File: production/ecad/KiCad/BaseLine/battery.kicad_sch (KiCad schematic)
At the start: 16 parts, among them IC1 AP7362-33SP-13 (3.3V LDO), J2 Conn_01x02, Q1 Si3456DDV, U7 LTC3872ETS8TRMPBF

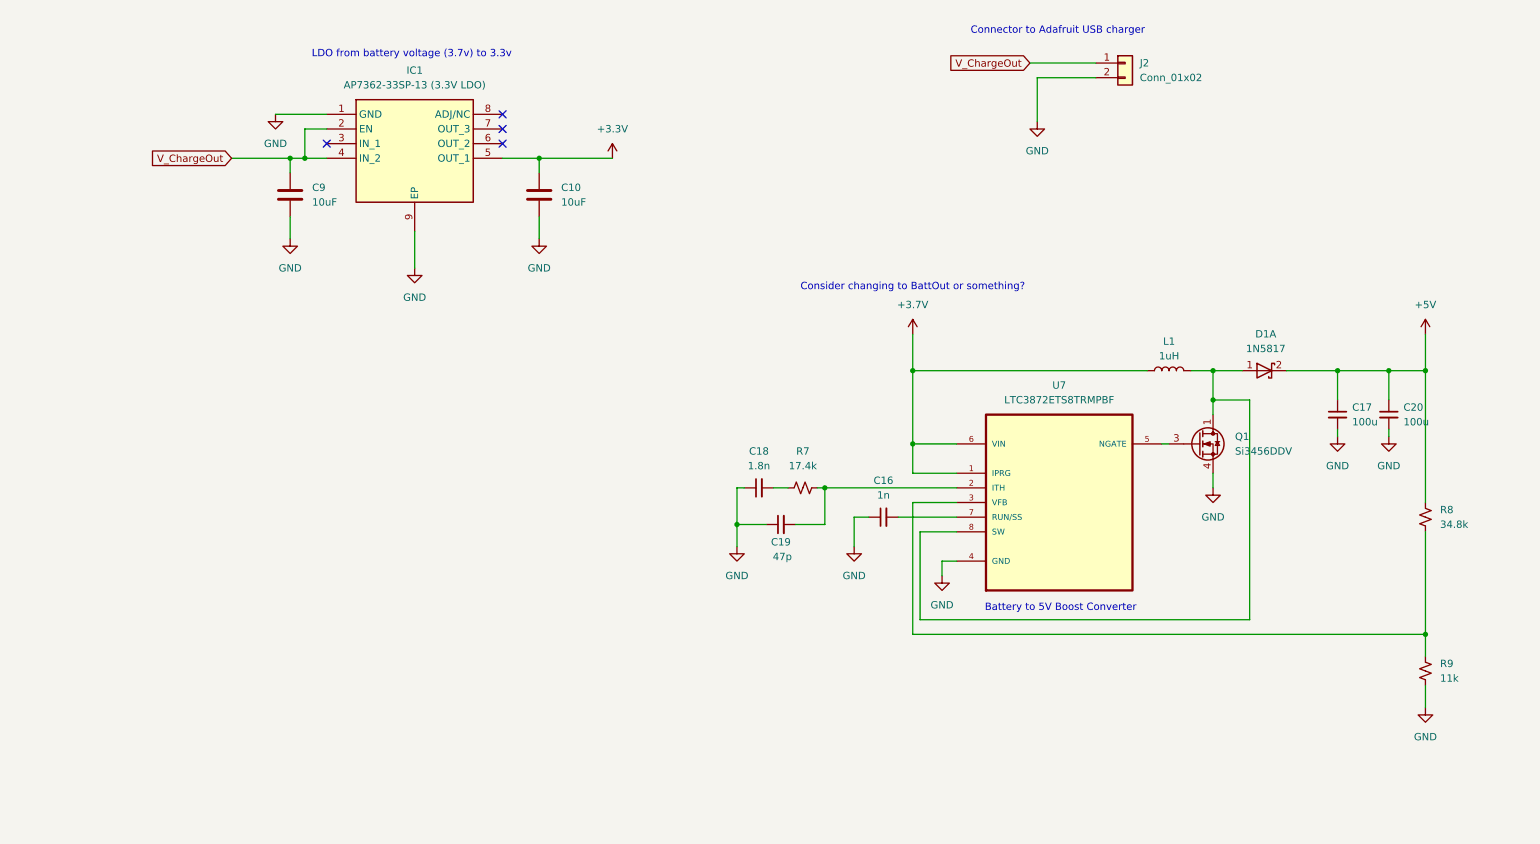
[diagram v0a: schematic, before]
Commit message: Added some zener diodes to BMS
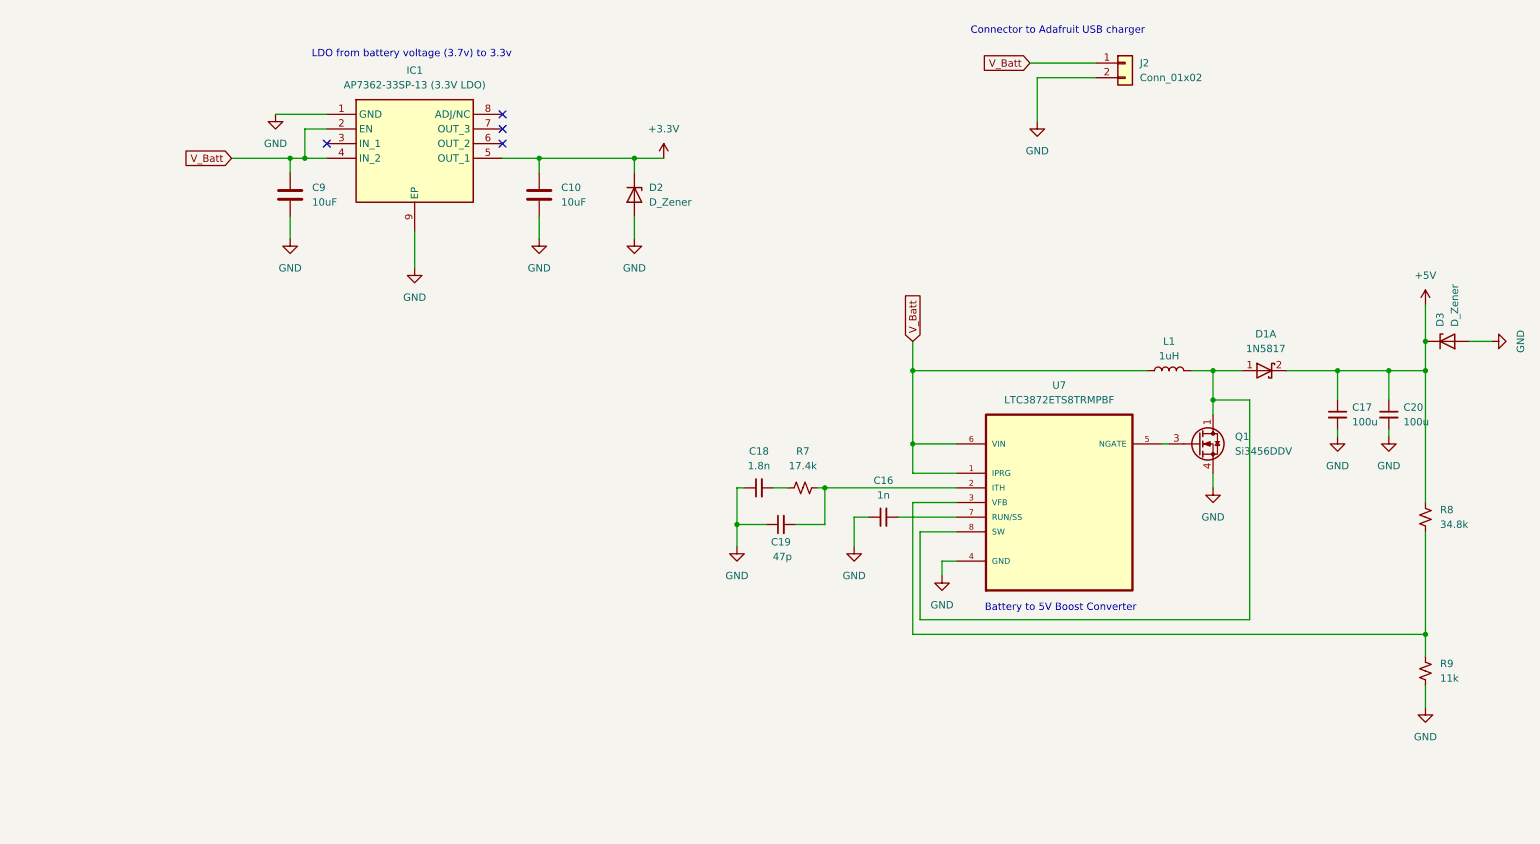
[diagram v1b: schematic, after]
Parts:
- added D2, D3: D_Zener, symbol Device:D_Zener
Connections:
- net V_ChargeOut is gone; now on net V_Batt: C9.2, IC1.2 (EN), IC1.4 (IN_2), J2.1 (Pin_1)
- net +3.3V: now also D2.1 (K)
- net +5V: now also D3.1 (K)
- net GND: now also D2.2 (A), D3.2 (A)
- net +3.7V renamed V_Batt
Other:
- note removed: "Consider changing to BattOut or something?"

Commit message: Started adding power button on BMS but needs additional info.
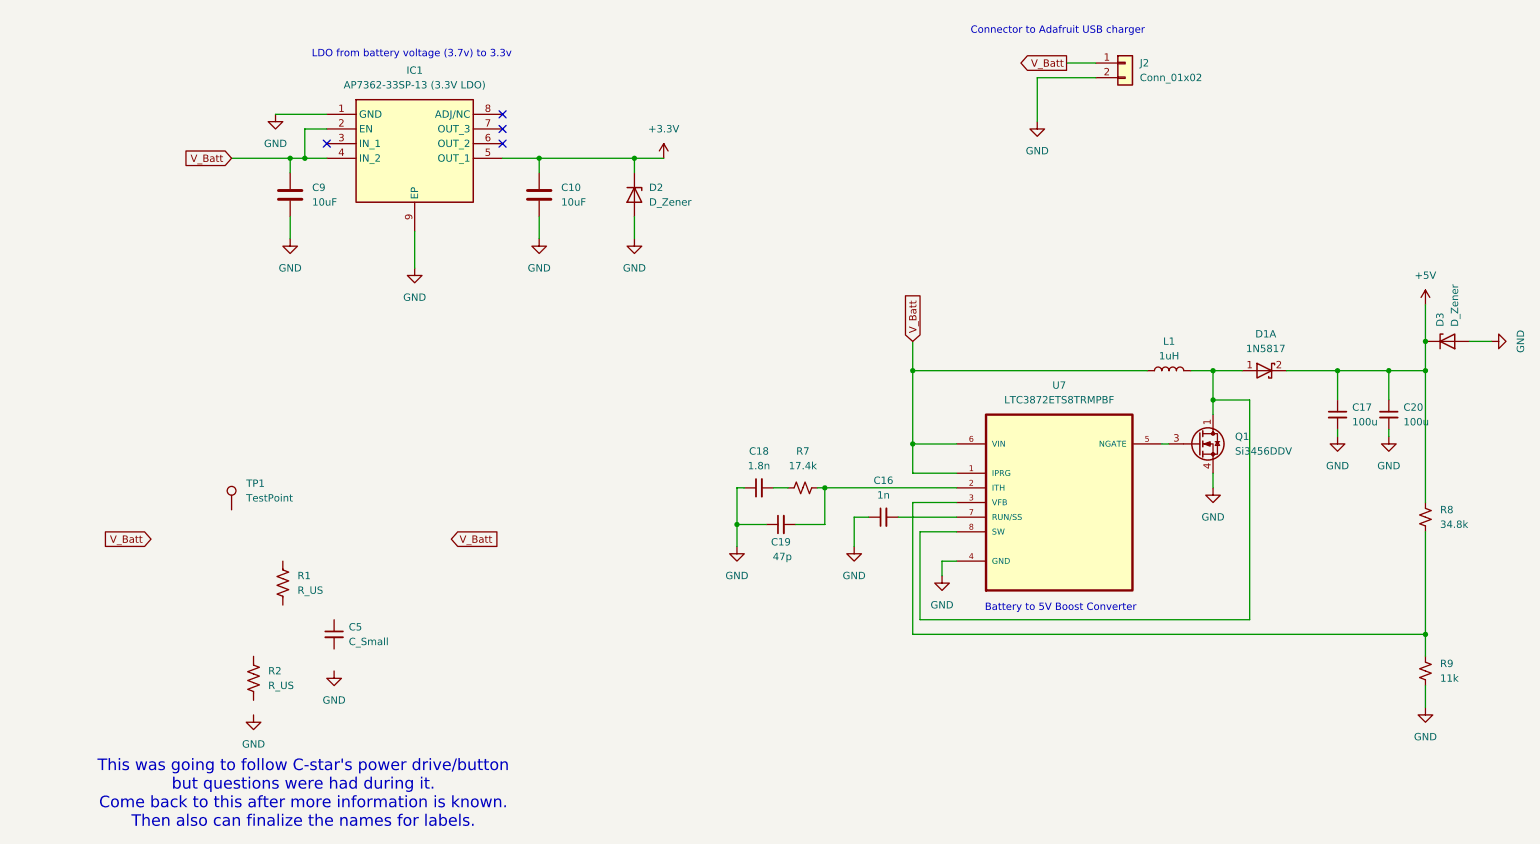
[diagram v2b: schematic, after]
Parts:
- added C5: C_Small, symbol Device:C_Small
- added R1, R2: R_US, symbol Device:R_US
- added TP1: TestPoint, symbol Connector:TestPoint
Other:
- note added: "This was going to follow C-star's power drive/button but questions were had during it. Come back to this after more information is known. Then also can finalize the names for labels."

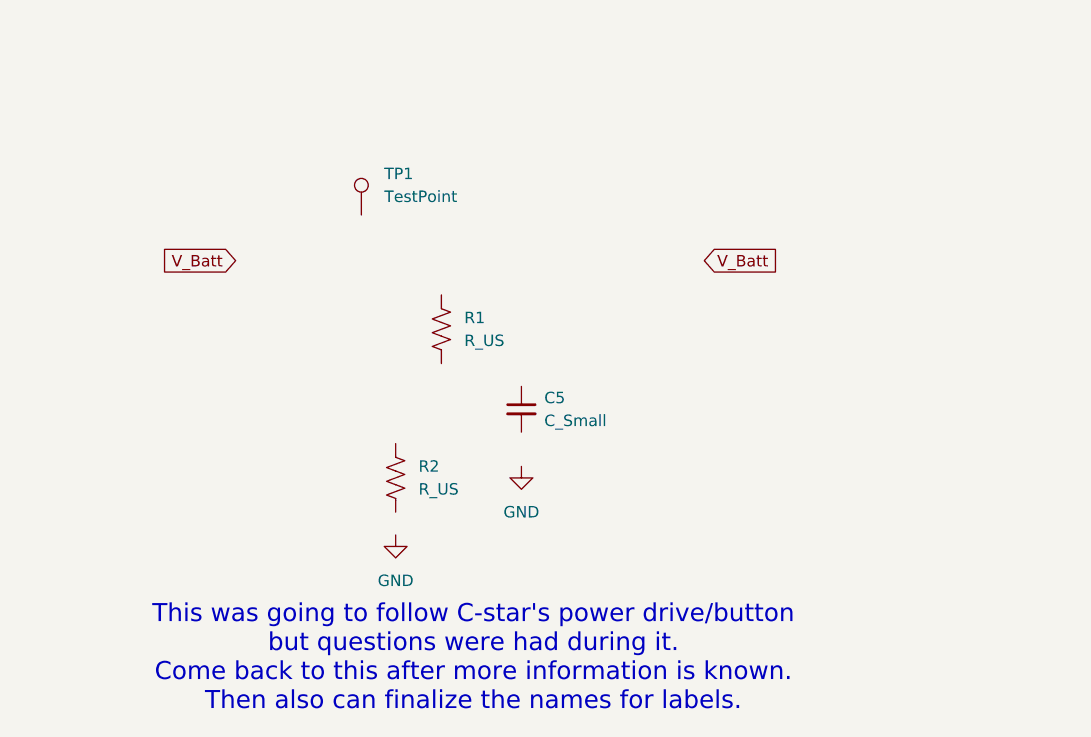
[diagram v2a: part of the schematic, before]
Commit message: MCU connections and matching names
matched the global net names of all the sensor connections with the MCU. Added an IO sheet for the power button
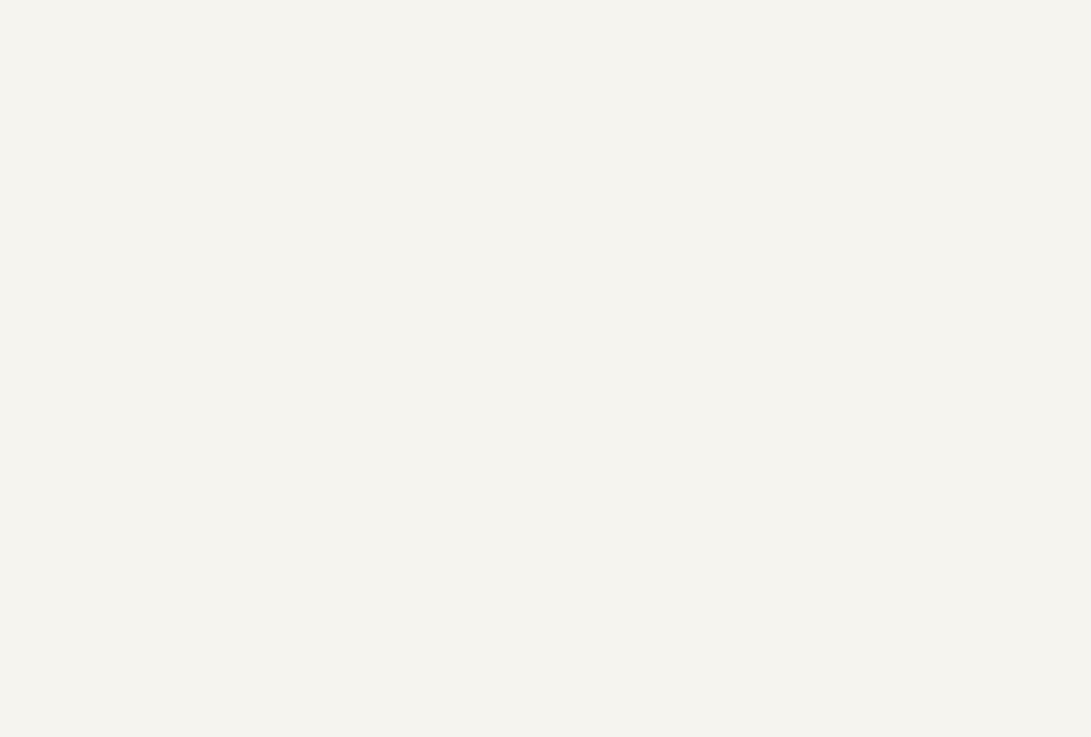
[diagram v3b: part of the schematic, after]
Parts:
- removed C5: C_Small, symbol Device:C_Small
- removed R1, R2: R_US, symbol Device:R_US
- removed TP1: TestPoint, symbol Connector:TestPoint
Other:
- note removed: "This was going to follow C-star's power drive/button but questions were had during it. Come back to this after more information is known. Then also can finalize the names for labels."

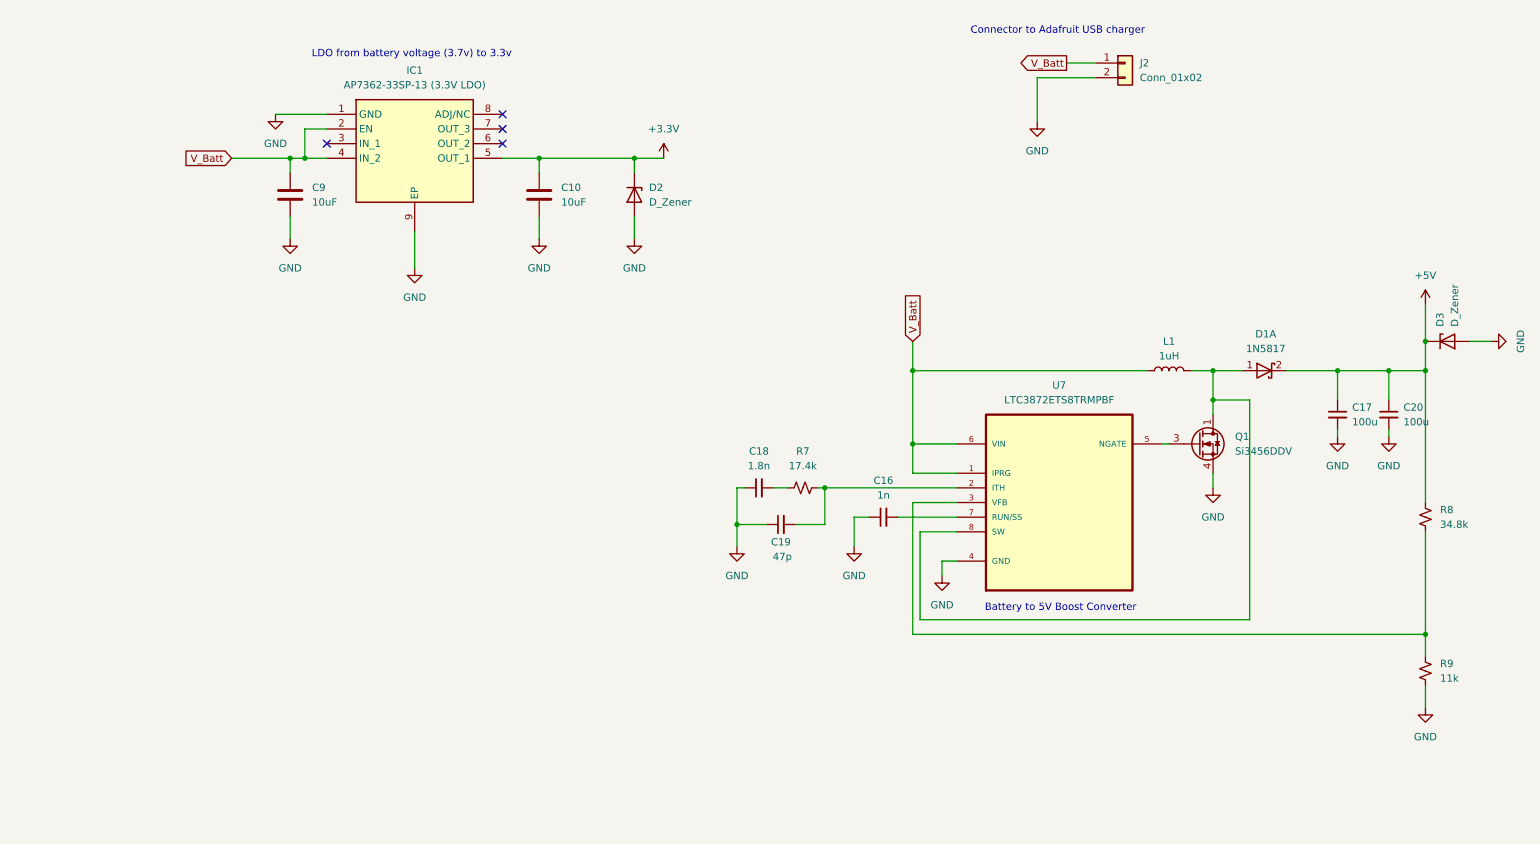
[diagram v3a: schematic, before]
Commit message: Added test points
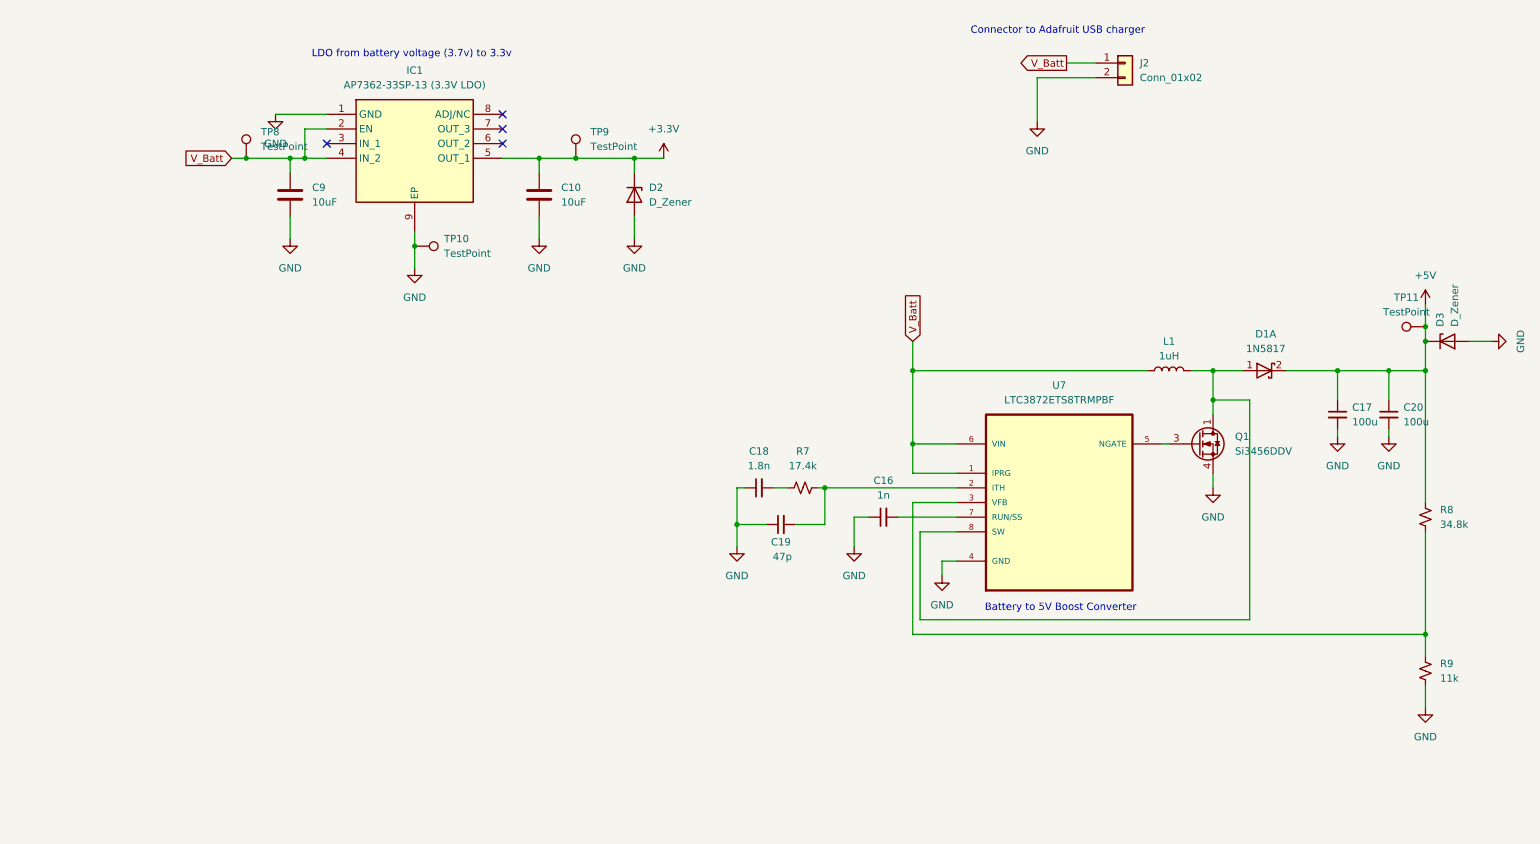
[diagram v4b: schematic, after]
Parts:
- added TP10, TP11, TP8, TP9: TestPoint, symbol Connector:TestPoint
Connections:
- net +3.3V: now also TP9.1
- net +5V: now also TP11.1
- net GND: now also TP10.1
- net V_Batt: now also TP8.1

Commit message: Changed annotations
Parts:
- renumbered C9 to C10, C10 to C11, C18 to C12, C19 to C13, C16 to C14, C17 to C15, C20 to C16, D2 to D1, D1 to D2, J2 to J3, Q1 to Q3, R7 to R29, R8 to R30, R9 to R31, TP8 to TP10, TP10 to TP11, TP9 to TP12, TP11 to TP13, U7 to U5

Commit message: More updated annotations and stuff
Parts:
- renumbered R29 to R32, R30 to R33, R31 to R34
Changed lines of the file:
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@@
 		(dnp no)
 		(fields_autoplaced yes)
-		(property "Reference" "R31"
+		(property "Reference" "R34"
 			(at 256.54 139.6999 0)
 			(effects
@@
 			(project "BaseLine"
 				(path "/ba9eda21-3882-41e1-8265-3d8ac781da20/31f727a4-3278-43bf-88f9-c0e8e93f0a52"
-					(reference "R31")
+					(reference "R34")
 					(unit 1)
 				)
@@
 		(dnp no)
 		(fields_autoplaced yes)
-		(property "Reference" "R30"
+		(property "Reference" "R33"
 			(at 256.54 113.0299 0)
 			(effects
@@
 			(project "BaseLine"
 				(path "/ba9eda21-3882-41e1-8265-3d8ac781da20/31f727a4-3278-43bf-88f9-c0e8e93f0a52"
-					(reference "R30")
+					(reference "R33")
 					(unit 1)
 				)
@@
 		(dnp no)
 		(fields_autoplaced yes)
-		(property "Reference" "R29"
+		(property "Reference" "R32"
 			(at 146.05 102.87 90)
 			(effects
@@
 			(project ""
 				(path "/ba9eda21-3882-41e1-8265-3d8ac781da20/31f727a4-3278-43bf-88f9-c0e8e93f0a52"
-					(reference "R29")
-					(unit 1)
-				)
+					(reference "R32")
+					(unit 1)
+				)
